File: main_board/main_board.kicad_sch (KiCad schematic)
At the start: 10 parts

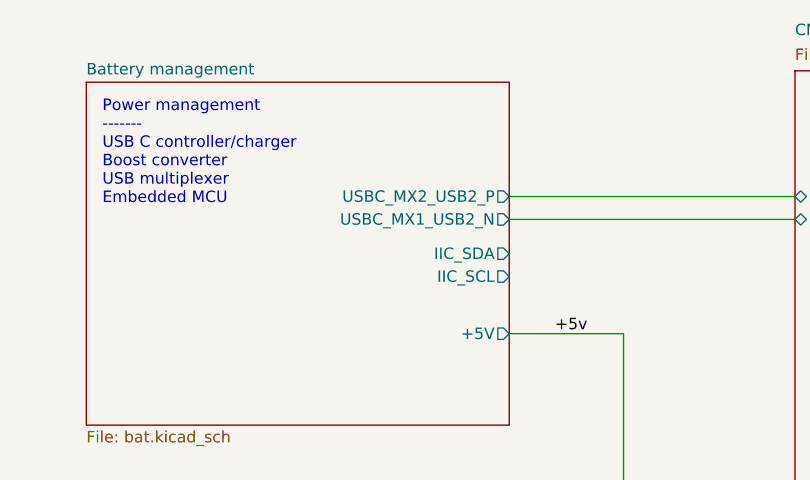
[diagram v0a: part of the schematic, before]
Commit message: Implement part of power management.
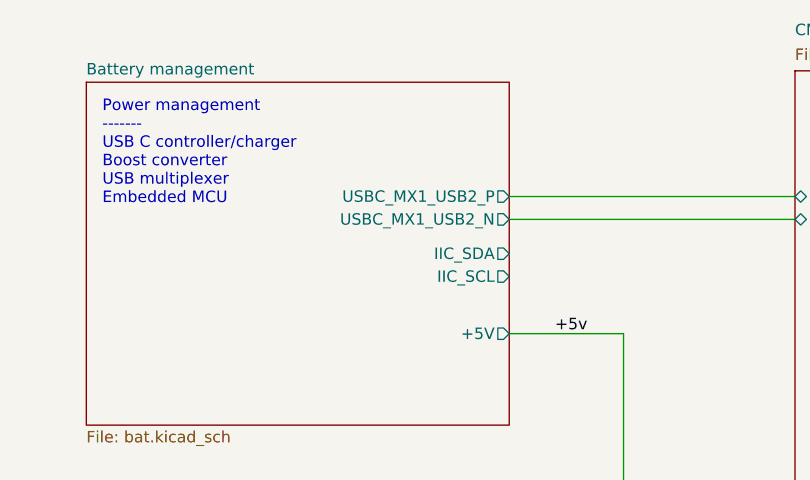
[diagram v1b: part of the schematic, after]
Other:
- sheet Battery management ports: added USBC_MX1_USB2_P; removed USBC_MX2_USB2_P
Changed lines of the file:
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@@
 		)
 		(instances
-			(project "dev_io_3"
+			(project "main_board"
 				(path "/e63e39d7-6ac0-4ffd-8aa3-1841a4541b55"
 					(page "3")
@@
 		)
 		(instances
-			(project "dev_io_3"
+			(project "main_board"
 				(path "/e63e39d7-6ac0-4ffd-8aa3-1841a4541b55"
 					(page "2")
@@
 		)
 		(instances
-			(project "dev_io_3"
+			(project "main_board"
 				(path "/e63e39d7-6ac0-4ffd-8aa3-1841a4541b55"
 					(page "4")
@@
 			)
 		)
-		(pin "USBC_MX2_USB2_P" output
+		(pin "USBC_MX1_USB2_P" output
 			(at 82.55 57.15 0)
 			(effects
@@
 		)
 		(instances
-			(project "dev_io_3"
+			(project "main_board"
 				(path "/e63e39d7-6ac0-4ffd-8aa3-1841a4541b55"
 					(page "5")

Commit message: More power management goodness
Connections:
- net +5v renamed Battery management/+5V
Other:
- sheet CM5_GPIO ports: added +5V, CM5_SCL, CM5_SDA; removed +3.3v, +5v
- sheet CM5_HighSpeed ports: added +5V; removed +3.3v, +5v
- sheet PCIe-M2 ports: added +5V; removed +5v
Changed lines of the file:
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@@
+	(wire
+		(pts
+			(xy 102.87 139.7) (xy 132.08 139.7)
+		)
+		(stroke
+			(width 0)
+			(type default)
+		)
+	)
 	(wire
 		(pts
@@
 	(wire
 		(pts
+			(xy 102.87 66.04) (xy 102.87 139.7)
+		)
+		(stroke
+			(width 0)
+			(type default)
+		)
+	)
+	(wire
+		(pts
+			(xy 105.41 137.16) (xy 105.41 63.5)
+		)
+		(stroke
+			(width 0)
+			(type default)
+		)
+	)
+	(wire
+		(pts
 			(xy 171.45 81.28) (xy 199.39 81.28)
 		)
@@
 	(wire
 		(pts
-			(xy 142.24 105.41) (xy 142.24 121.92)
+			(xy 105.41 63.5) (xy 82.55 63.5)
+		)
+		(stroke
+			(width 0)
+			(type default)
+		)
+	)
+	(wire
+		(pts
+			(xy 82.55 66.04) (xy 102.87 66.04)
+		)
+		(stroke
+			(width 0)
+			(type default)
+		)
+	)
+	(wire
+		(pts
+			(xy 132.08 137.16) (xy 105.41 137.16)
 		)
 		(stroke
@@
 	(text "Connectors\n-------\n40way RPI\nJumpers\nFan\nBattery"
 		(exclude_from_sim no)
-		(at 141.224 144.018 0)
+		(at 145.796 144.526 0)
 		(effects
 			(font
@@
 		(exclude_from_sim no)
 		(at 134.62 67.31 0)
-		(effects
-			(font
-				(size 1.27 1.27)
-			)
-			(justify left bottom)
-		)
-	)
-	(label "+5v"
-		(at 87.63 72.39 0)
-		(fields_autoplaced yes)
 		(effects
 			(font
@@
 			)
 		)
-		(pin "+5v" input
+		(pin "+5V" input
 			(at 149.86 121.92 90)
 			(effects
@@
 			)
 		)
-		(pin "+3.3v" output
-			(at 142.24 121.92 90)
-			(effects
-				(font
-					(size 1.27 1.27)
-				)
-				(justify right)
+		(pin "CM5_SDA" output
+			(at 132.08 137.16 180)
+			(effects
+				(font
+					(size 1.27 1.27)
+				)
+				(justify left)
+			)
+		)
+		(pin "CM5_SCL" output
+			(at 132.08 139.7 180)
+			(effects
+				(font
+					(size 1.27 1.27)
+				)
+				(justify left)
 			)
 		)
@@
 			)
 		)
-		(pin "+5v" input
+		(pin "+5V" input
 			(at 149.86 105.41 270)
 			(effects
@@
 				)
 				(justify right)
-			)
-		)
-		(pin "+3.3v" input
-			(at 142.24 105.41 270)
-			(effects
-				(font
-					(size 1.27 1.27)
-				)
-				(justify left)
 			)
 		)
@@
 			)
 		)
-		(pin "+5v" input
+		(pin "+5V" input
 			(at 214.63 95.25 270)
 			(effects

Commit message: Finalize power management
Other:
- added sheet USB hub (USB_hub.kicad_sch)
- sheet Battery management ports: added CM5_PMIC_EN; removed none
- sheet CM5_GPIO ports: added CM5_PMIC_EN; removed none
- moved on the sheet: C18, C9

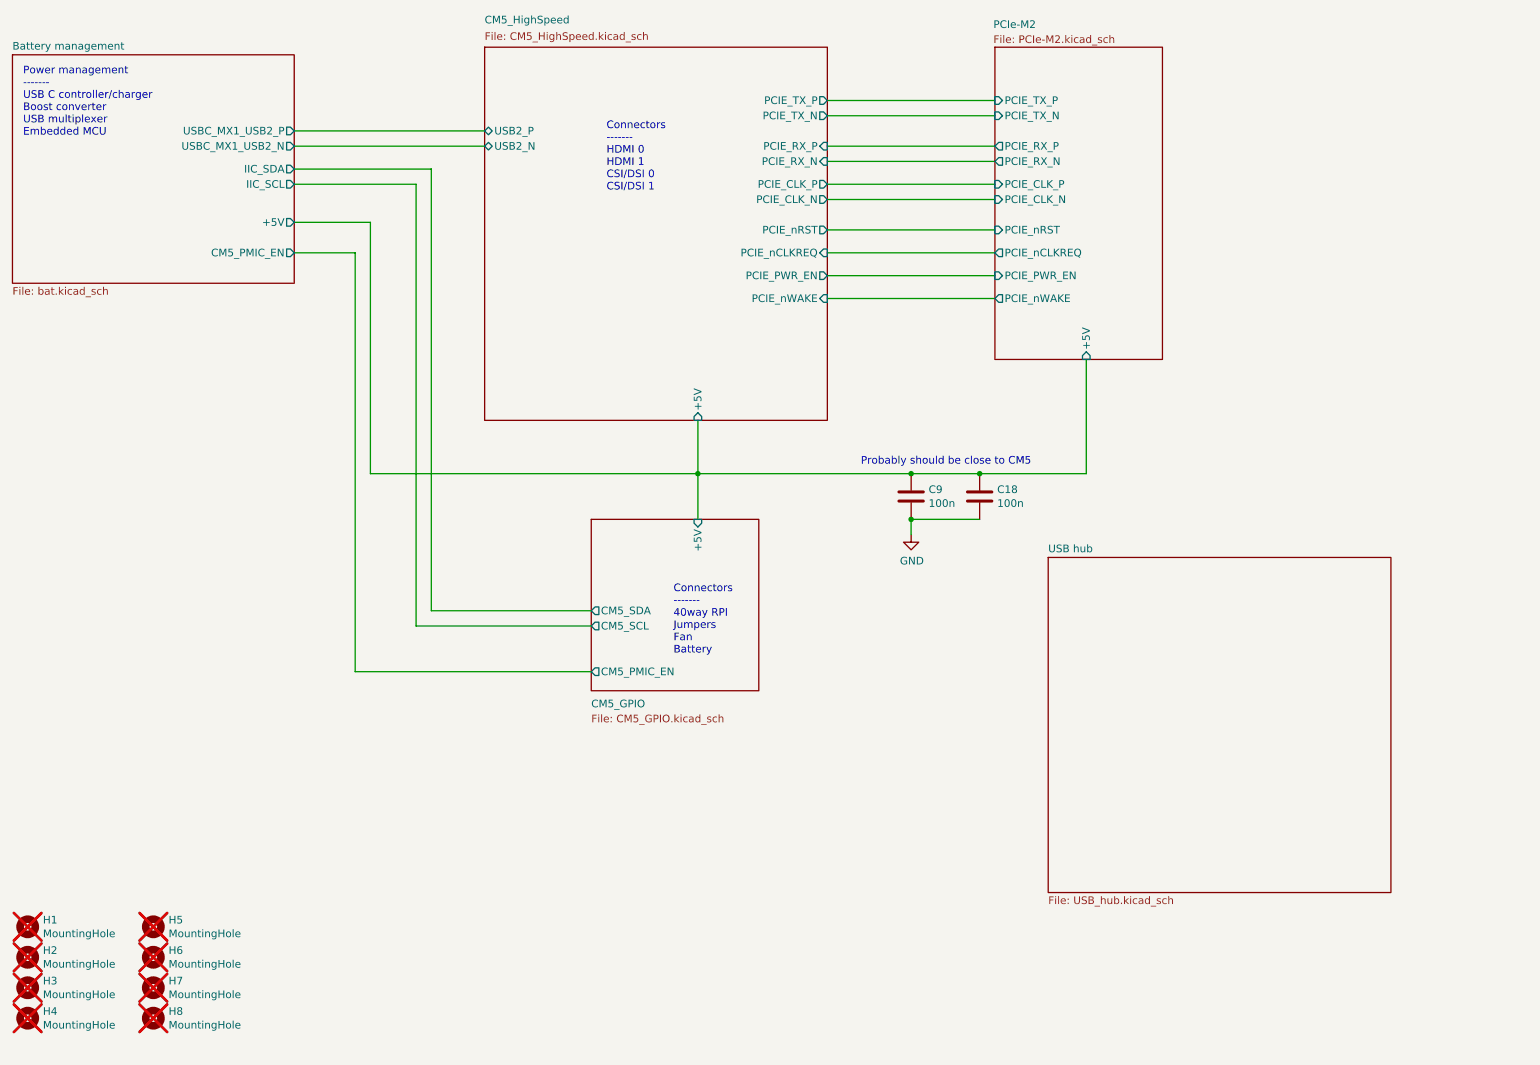
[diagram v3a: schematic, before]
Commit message: Start reouting USB hub
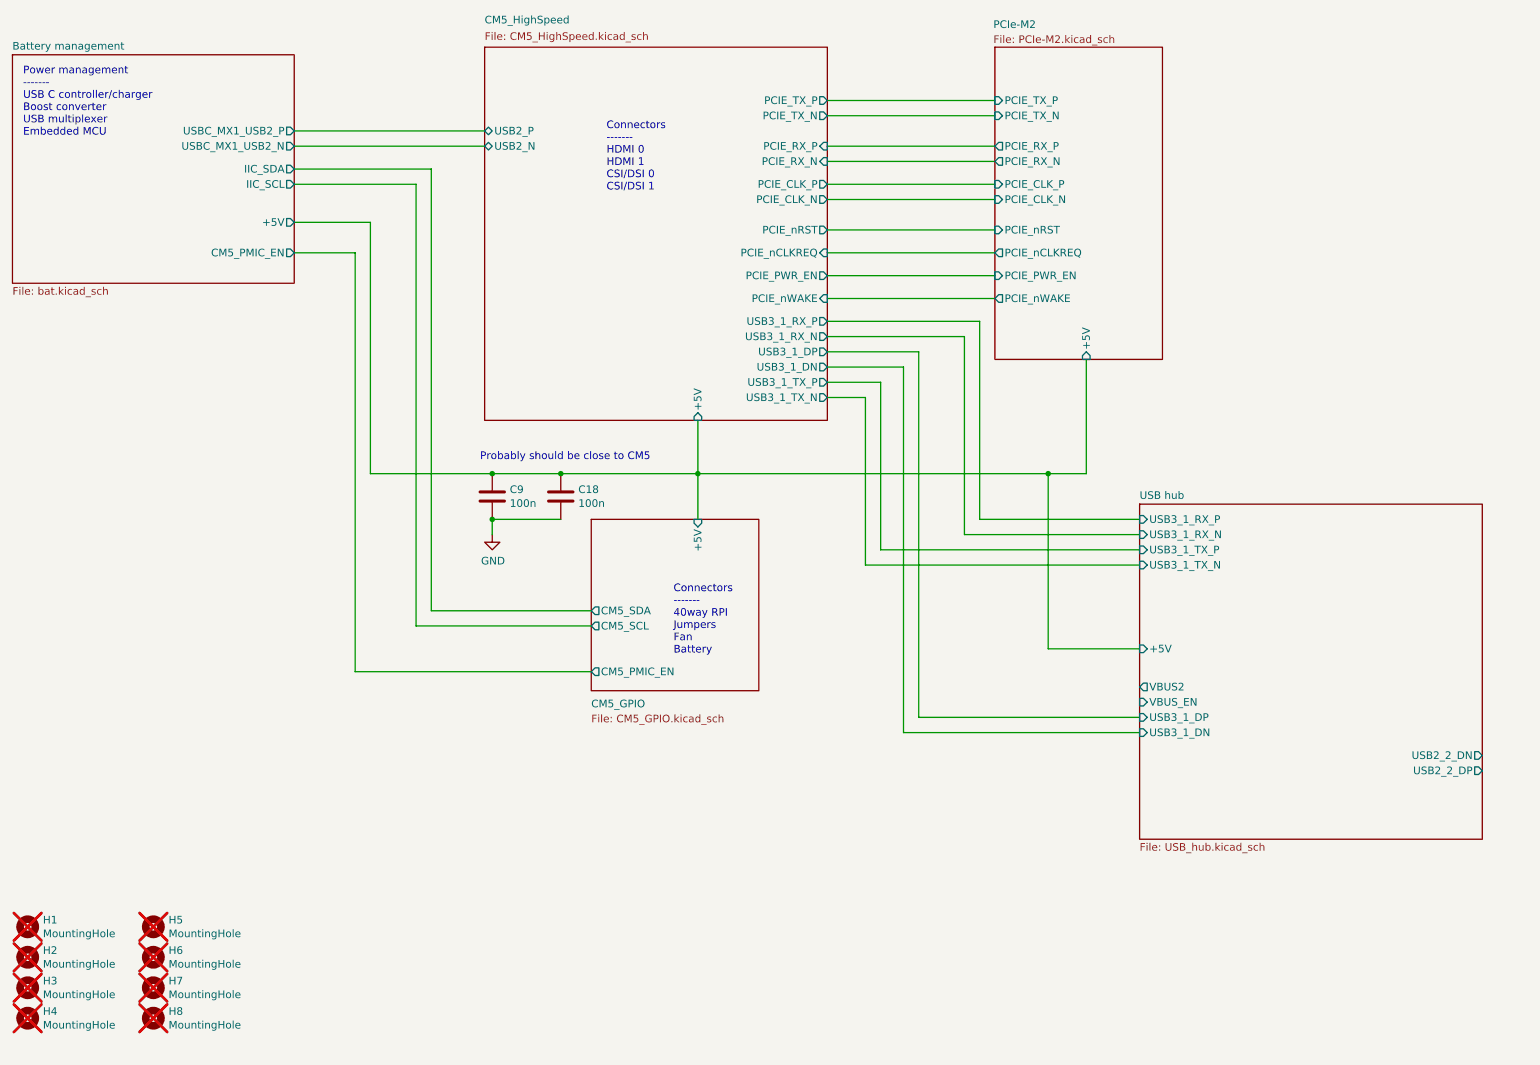
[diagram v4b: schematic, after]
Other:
- sheet CM5_HighSpeed ports: added USB3_1_DN, USB3_1_DP, USB3_1_RX_N, USB3_1_RX_P, USB3_1_TX_N, USB3_1_TX_P; removed none
- sheet USB hub ports: added +5V, USB2_2_DN, USB2_2_DP, USB3_1_DN, USB3_1_DP, USB3_1_RX_N, USB3_1_RX_P, USB3_1_TX_N, USB3_1_TX_P, VBUS2, VBUS_EN; removed none
- moved on the sheet: C18, C9

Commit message: Bunch more routing, mainly added MIPI interface, reworked power management a bit
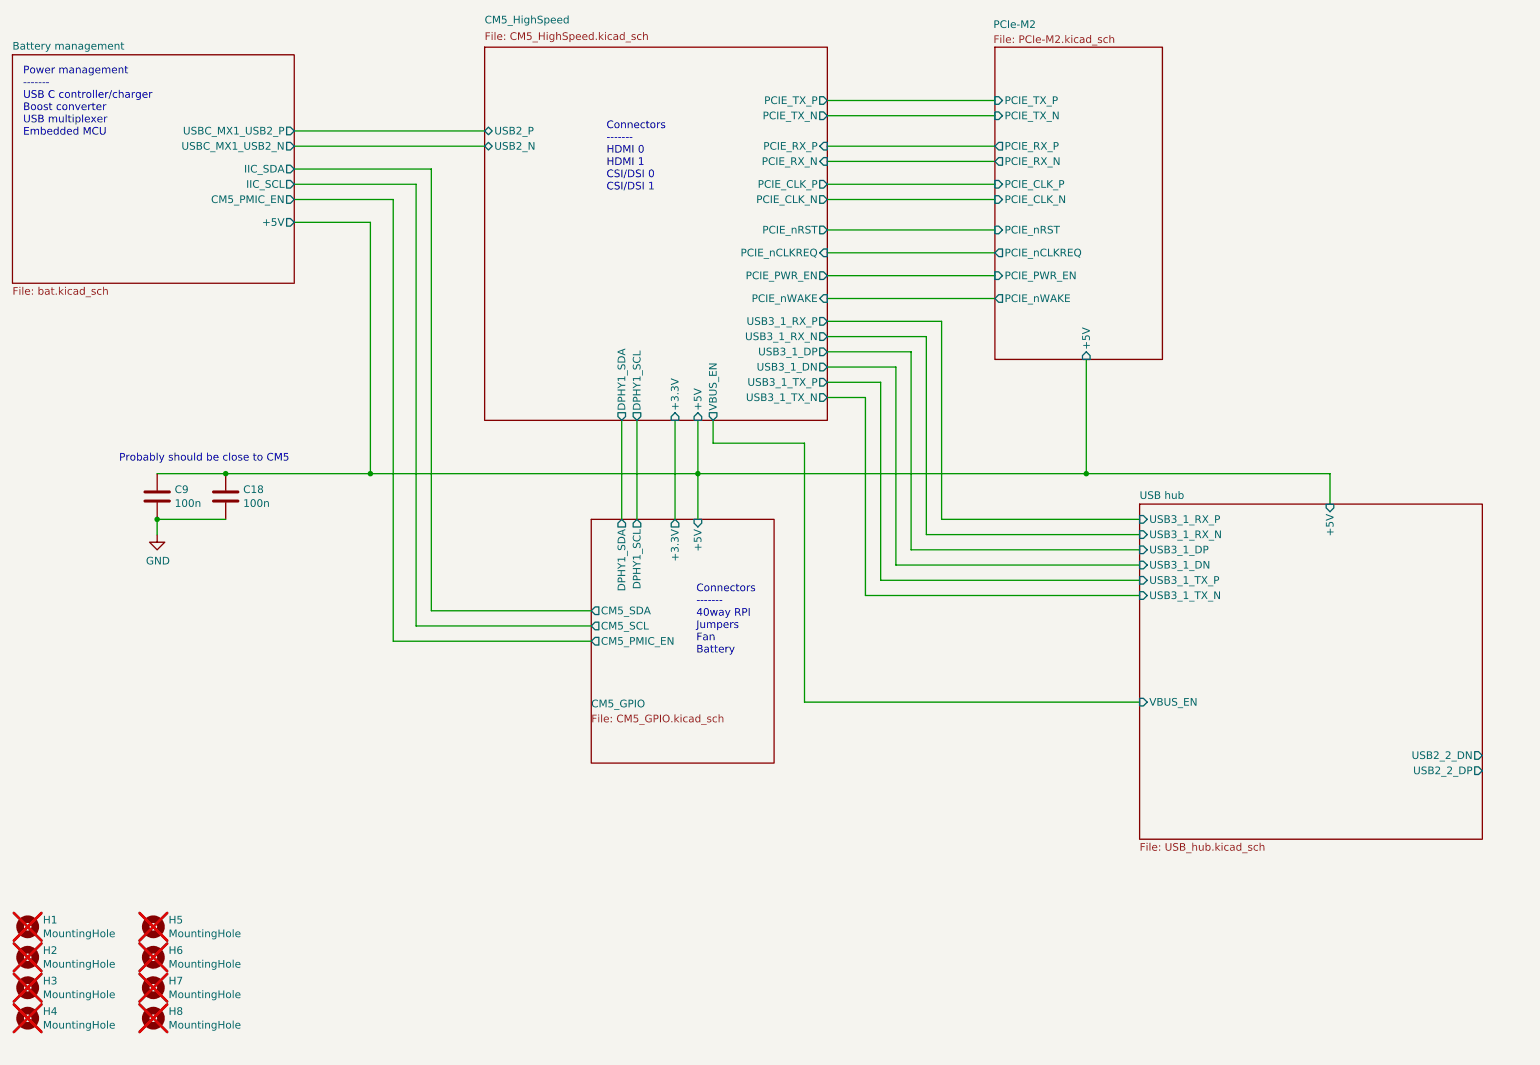
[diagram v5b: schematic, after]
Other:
- sheet CM5_GPIO ports: added +3.3V, DPHY1_SCL, DPHY1_SDA; removed none
- sheet CM5_HighSpeed ports: added +3.3V, DPHY1_SCL, DPHY1_SDA, VBUS_EN; removed none
- sheet USB hub ports: added none; removed VBUS2
- moved on the sheet: C18, C9

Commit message: Bunch of fixes + audio out interface
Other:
- sheet Battery management ports: added 3.3v; removed CM5_PMIC_EN
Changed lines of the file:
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@@
+	)
+	(junction
+		(at 130.81 87.63)
+		(diameter 0)
+		(color 0 0 0 0)
 	)
 	(junction
@@
 	(wire
 		(pts
-			(xy 83.82 44.45) (xy 83.82 118.11)
-		)
-		(stroke
-			(width 0)
-			(type default)
-		)
-	)
-	(wire
-		(pts
 			(xy 124.46 81.28) (xy 124.46 97.79)
 		)
@@
 	(wire
 		(pts
+			(xy 77.47 50.8) (xy 67.31 50.8)
+		)
+		(stroke
+			(width 0)
+			(type default)
+		)
+	)
+	(wire
+		(pts
 			(xy 156.21 41.91) (xy 184.15 41.91)
 		)
@@
 	(wire
 		(pts
-			(xy 83.82 118.11) (xy 116.84 118.11)
-		)
-		(stroke
-			(width 0)
-			(type default)
-		)
-	)
-	(wire
-		(pts
 			(xy 156.21 49.53) (xy 184.15 49.53)
 		)
@@
 	(wire
 		(pts
+			(xy 130.81 87.63) (xy 130.81 97.79)
+		)
+		(stroke
+			(width 0)
+			(type default)
+		)
+	)
+	(wire
+		(pts
 			(xy 152.4 128.27) (xy 208.28 128.27)
 		)
@@
 	(wire
 		(pts
-			(xy 67.31 44.45) (xy 83.82 44.45)
-		)
-		(stroke
-			(width 0)
-			(type default)
-		)
-	)
-	(wire
-		(pts
 			(xy 172.72 67.31) (xy 172.72 100.33)
 		)
@@
 	(wire
 		(pts
+			(xy 130.81 87.63) (xy 77.47 87.63)
+		)
+		(stroke
+			(width 0)
+			(type default)
+		)
+	)
+	(wire
+		(pts
 			(xy 137.16 81.28) (xy 137.16 85.09)
 		)
@@
 	(wire
 		(pts
+			(xy 77.47 87.63) (xy 77.47 50.8)
+		)
+		(stroke
+			(width 0)
+			(type default)
+		)
+	)
+	(wire
+		(pts
 			(xy 170.18 69.85) (xy 170.18 102.87)
 		)
@@
 	(wire
 		(pts
-			(xy 130.81 81.28) (xy 130.81 97.79)
+			(xy 130.81 81.28) (xy 130.81 87.63)
 		)
 		(stroke
@@
 			)
 		)
-		(pin "CM5_PMIC_EN" output
-			(at 67.31 44.45 0)
-			(effects
-				(font
+		(pin "3.3v" output
+			(at 67.31 50.8 0)
+			(effects
+				(font

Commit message: Implement power monitoring
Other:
- note added: "Connectors ------- HDMI CSI/DSI USB"
- note added: "Connectors ------- Sound interface"
- note added: "Power management ------- USB C controller/charger Boost converter USB multiplexer Embedded MCU Power metering"
- note removed: "Connectors ------- 40way RPI Jumpers Fan Battery"
- note removed: "Connectors ------- HDMI 0 HDMI 1 CSI/DSI 0 CSI/DSI 1"
- note removed: "Power management ------- USB C controller/charger Boost converter USB multiplexer Embedded MCU"
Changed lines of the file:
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@@
 		)
 	)
-	(text "Connectors\n-------\n40way RPI\nJumpers\nFan\nBattery"
+	(text "Connectors\n-------\nSound interface\n"
 		(exclude_from_sim no)
-		(at 134.366 120.396 0)
+		(at 131.318 113.538 0)
 		(effects
 			(font
@@
 		)
 	)
-	(text "Power management\n-------\nUSB C controller/charger\nBoost converter\nUSB multiplexer\nEmbedded MCU\n"
+	(text "Power management\n-------\nUSB C controller/charger\nBoost converter\nUSB multiplexer\nEmbedded MCU\nPower metering\n"
 		(exclude_from_sim no)
-		(at 22.098 34.036 0)
+		(at 22.352 36.322 0)
 		(effects
 			(font
@@
 		)
 	)
-	(text "Connectors\n-------\nHDMI 0\nHDMI 1\nCSI/DSI 0\nCSI/DSI 1"
+	(text "Connectors\n-------\nHDMI\nCSI/DSI\nUSB\n"
 		(exclude_from_sim no)
 		(at 119.38 43.18 0)
